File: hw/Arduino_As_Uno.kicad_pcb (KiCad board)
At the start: 2 copper layers, 68.6 x 53.3 mm, 70 parts, among them CON1 BARREL_JACK, P1 USB_OTG, P10 CONN_01X06, P11 CONN_01X08, P13 CONN_02X03, P14 CONN_02X03_ICSP, P15 CONN_01X08, P2 CONN_02X03_ICSP, P22 CONN_02X03_ICSP, P3 CONN_02X03, P4 CONN_02X03_ICSP, P5 CONN_01X08, P6 CONN_02X03, P7 CONN_02X03_ICSP, P8 CONN_02X03_ICSP, P9 CONN_01X10, Q1 FDN340P, SW1 SW_PUSH, U1 LM2940LD-5.0, U10 TS3A44159, U11 FDG6331L, U2 MIC5205, U3 ATMEGA16U2, U4 23K256, U5 ATTINY85-SUR, U6 TS3A44159, U7 ATMEGA328PB-MU, U8 74LVCH1T45, U9 ATTINY85-SUR, X1 CRYSTAL, X2 RESONATOR

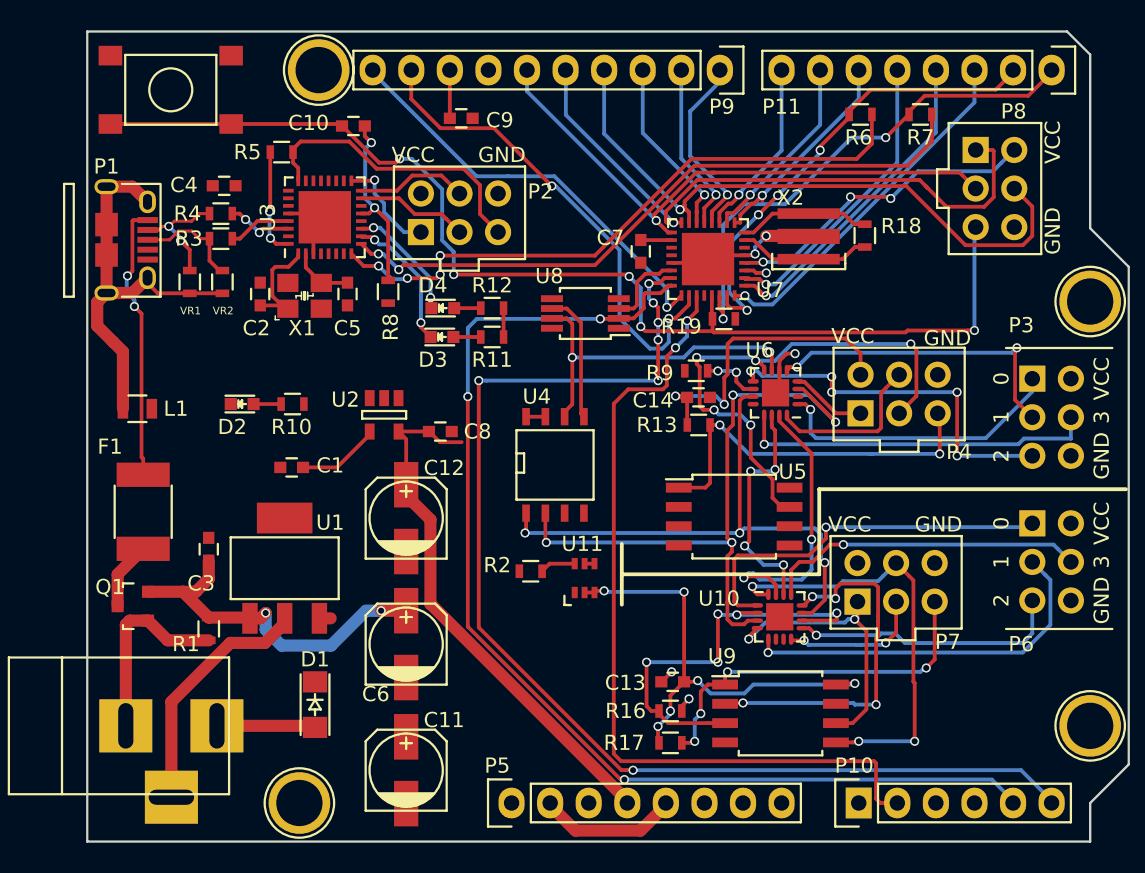
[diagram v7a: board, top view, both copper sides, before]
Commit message: cleaned up many traces, especially around QFNs and in the power area. Power traces are next.
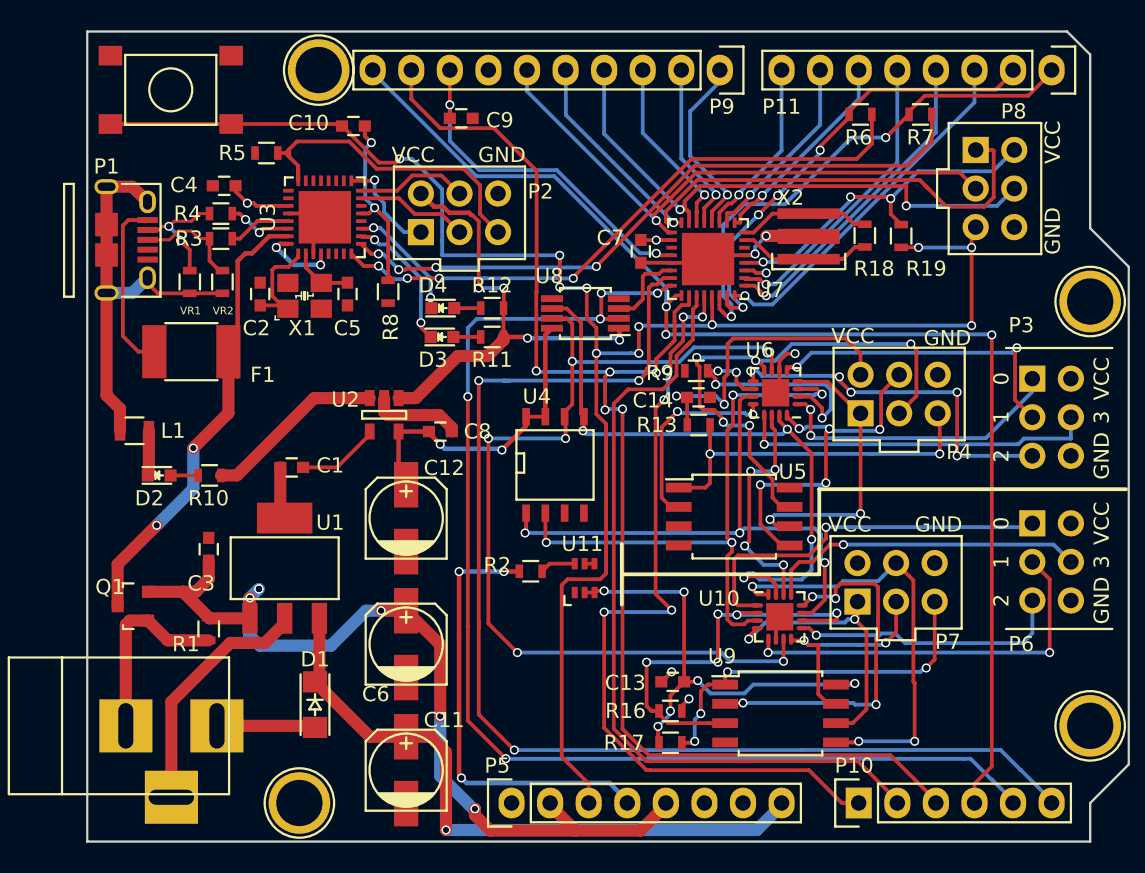
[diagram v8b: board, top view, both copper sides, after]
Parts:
- moved R19 12.9 mm to (164.6, 86.5), turned to 270 degrees
- moved F1 11.0 mm to (117.9, 94.1), turned to 0 degrees
- moved D2 7.20 mm to (115.7, 102.3)
- moved R10 7.20 mm to (119.1, 102.3)
- moved L1 1.46 mm to (114.1, 99.3)
- moved R5 1.00 mm to (122.8, 81.0)
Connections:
- P13 pad 1: /IO0_T2 -> GND
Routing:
- net +5V: track 65.3 -> 132.3 mm, vias 7 -> 16
- net /AD2/SDA: track 32.4 -> 87.2 mm, vias 2 -> 5
- net /AD3/SCL: track 28.5 -> 83.2 mm, vias 1 -> 3
- net /AD0: track 0.00 -> 54.3 mm, vias 0 -> 6
- net /VIN: track 1.44 -> 42.9 mm, vias 0 -> 1
- net /RST_328: track 76.5 -> 117.5 mm, vias 5 -> 11
- net /SCK_RAM: track 22.5 -> 63.3 mm, vias 2 -> 6
- net /USBVCC: track 4.47 -> 31.4 mm, vias 0 -> 2
- net /AREF: track 3.17 -> 23.3 mm, vias 0 -> 2
- net GND: track 35.0 -> 54.2 mm
- net +3V3: track 52.5 -> 67.5 mm, vias 4 -> 9
- net /MOSI_RAM: track 28.0 -> 42.6 mm, vias 2 -> 4
- net /MISO_T1: track 4.99 -> 19.2 mm, vias 0 -> 2
- net /SELECT_T1: track 3.89 -> 17.4 mm, vias 2 -> 4
- net /~SS~_T1: track 0.00 -> 13.2 mm, vias 0 -> 2
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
